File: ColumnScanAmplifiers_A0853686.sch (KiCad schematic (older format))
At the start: 0 parts

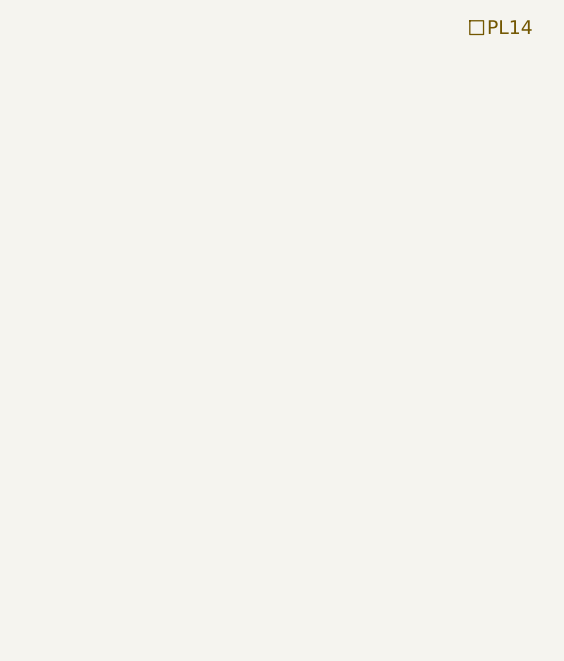
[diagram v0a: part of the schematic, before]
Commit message: Corrects mistakes in existing sub schematics
This corrections were done based on comparison with the actual paper
schematics.
Mainly renaming some pins, which were labled wrongly, plus addid of additional
pins (sockets) which had been overlooked.
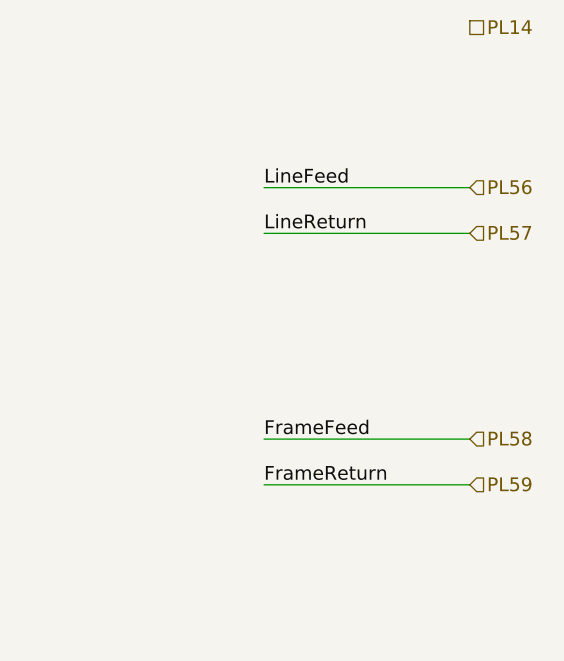
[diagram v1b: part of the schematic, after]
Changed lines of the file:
@@
 LIBS:contrib
 LIBS:valves
+LIBS:Stereoscan120-cache
 EELAYER 26 0
 EELAYER END
 $Descr A4 11693 8268
 encoding utf-8
-Sheet 6 11
+Sheet 6 12
 Title ""
 Date ""
@@
 Text Label 2300 5200 2    60   ~ 0
 YScanInput
+Text HLabel 10300 2000 2    60   Input ~ 0
+PL56
+Text HLabel 10300 2200 2    60   Input ~ 0
+PL57
+Text HLabel 10300 3100 2    60   Input ~ 0
+PL58
+Text HLabel 10300 3300 2    60   Input ~ 0
+PL59
+Wire Wire Line
+	10300 2000 9400 2000
+Wire Wire Line
+	10300 2200 9400 2200
+Wire Wire Line
+	10300 3100 9400 3100
+Wire Wire Line
+	10300 3300 9400 3300
+Text Label 9400 2000 0    60   ~ 0
+LineFeed
+Text Label 9400 2200 0    60   ~ 0
+LineReturn
+Text Label 9400 3100 0    60   ~ 0
+FrameFeed
+Text Label 9400 3300 0    60   ~ 0
+FrameReturn
 $EndSCHEMATC

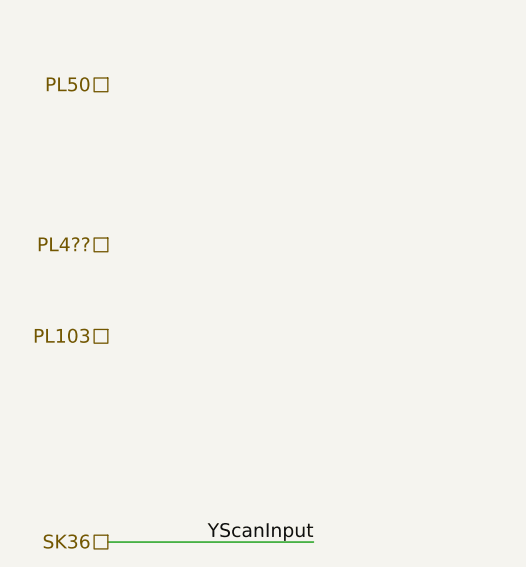
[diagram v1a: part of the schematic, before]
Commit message: Adds Line and Frame deflection inductances
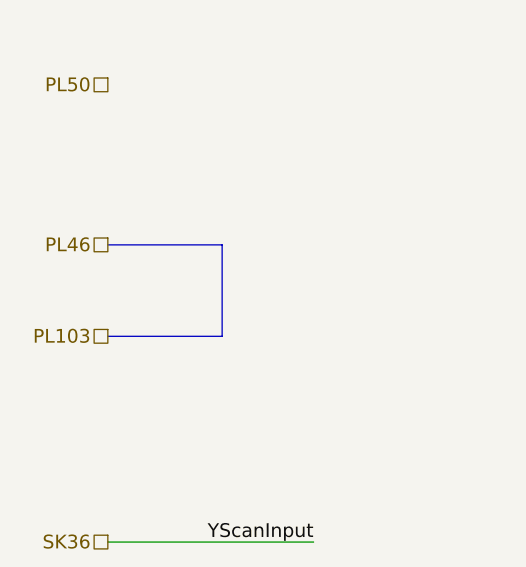
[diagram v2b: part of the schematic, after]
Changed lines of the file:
@@
 PL50
 Text HLabel 1400 3900 0    60   UnSpc ~ 0
-PL4??
+PL46
 Text HLabel 1400 4300 0    60   UnSpc ~ 0
 PL103
@@
 Text Label 9400 3300 0    60   ~ 0
 FrameReturn
+Wire Bus Line
+	1400 4300 1900 4300
+Wire Bus Line
+	1900 4300 1900 3900
+Wire Bus Line
+	1900 3900 1400 3900
 $EndSCHEMATC
